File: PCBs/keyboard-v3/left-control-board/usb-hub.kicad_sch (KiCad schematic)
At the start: 16 parts, among them U101 USB2534-1080AEN, U801 NCP380HMU05AATBG, Y101 CX2016SA24000D0HLLG3

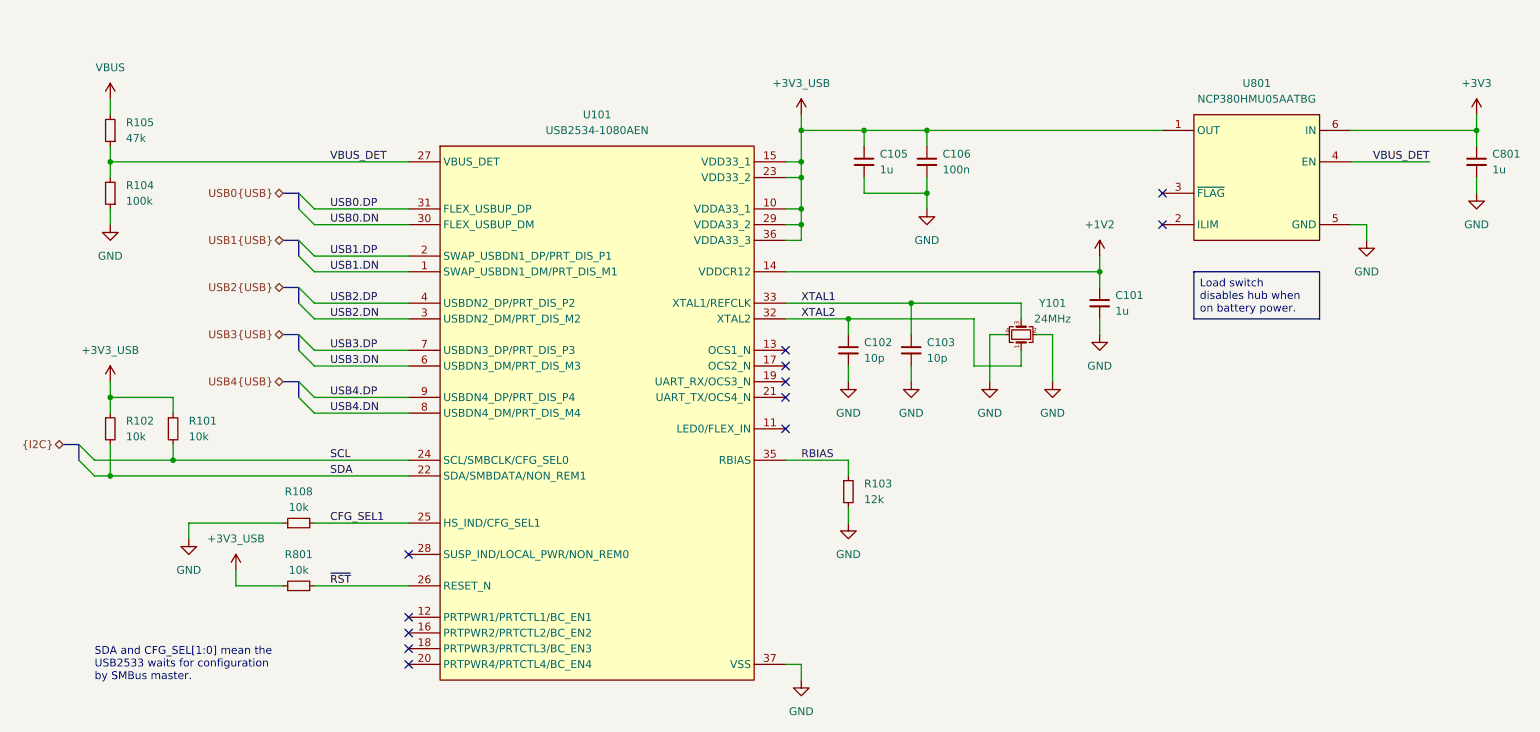
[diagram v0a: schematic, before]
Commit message: Added debug-breakout board, progress on right side schematics & layout
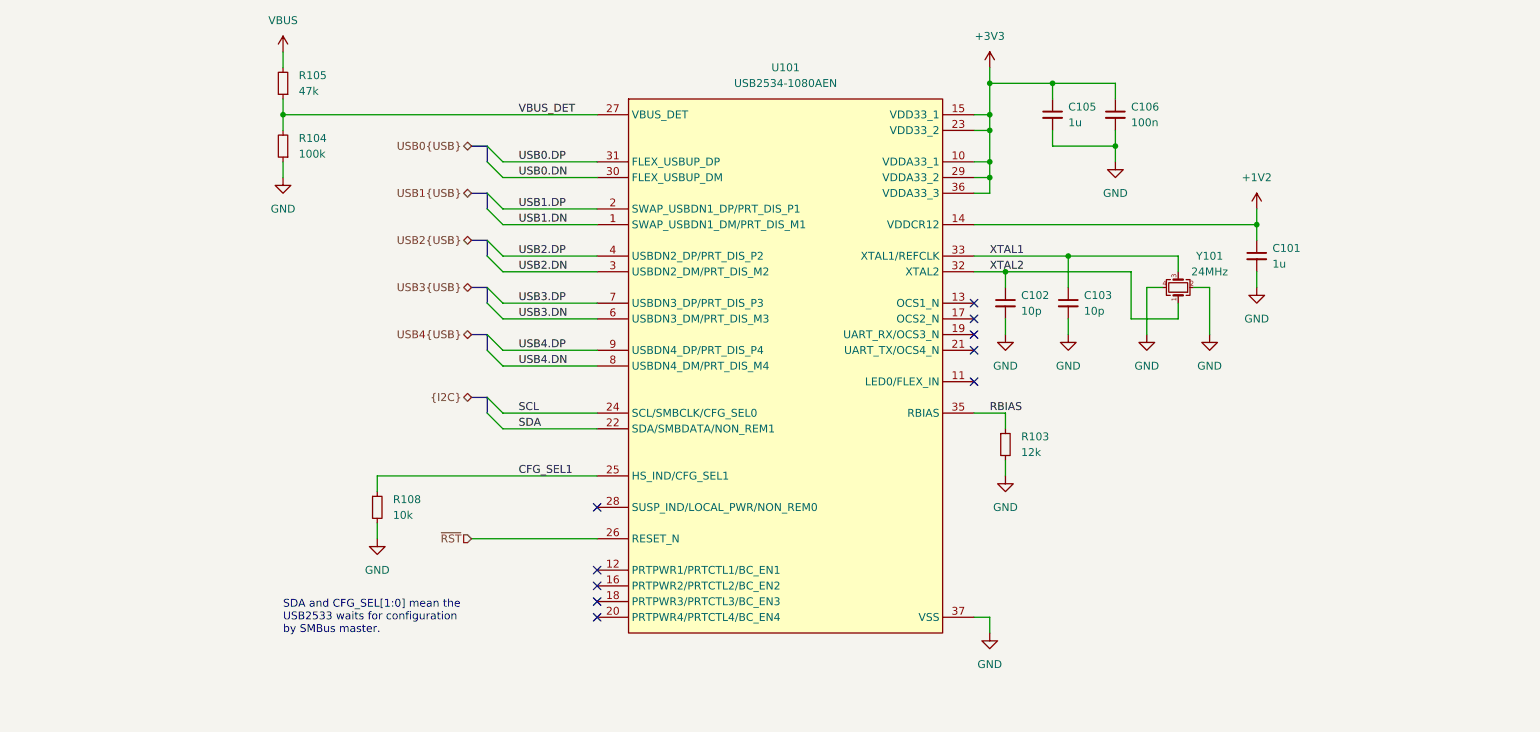
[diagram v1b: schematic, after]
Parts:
- removed C801: 1u, project_footprints:C_0402, symbol DEV:C_SMALL
- removed R101, R102, R801: 10k, project_footprints:R_0402, symbol DEV:R_SMALL
- removed U801: NCP380HMU05AATBG, project_footprints:SON65P200X200X55-7N, symbol PWR-SWCH:NCP380HMU05AATBG
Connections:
- net +3V3_USB is gone; now on net +3V3: C105.1, C106.1, U101.10 (VDDA33_1), U101.15 (VDD33_1), U101.23 (VDD33_2), U101.29 (VDDA33_2), U101.36 (VDDA33_3)
- net CFG_SEL1: now also R108.1; no longer R108.2
- net GND: now also R108.2; no longer R108.1
- no-connect marks 12 -> 10
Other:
- moved on the sheet: C101, C102, C103, C105, C106, R103, R104, R105, R108, U101, Y101

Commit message: Left knob board done
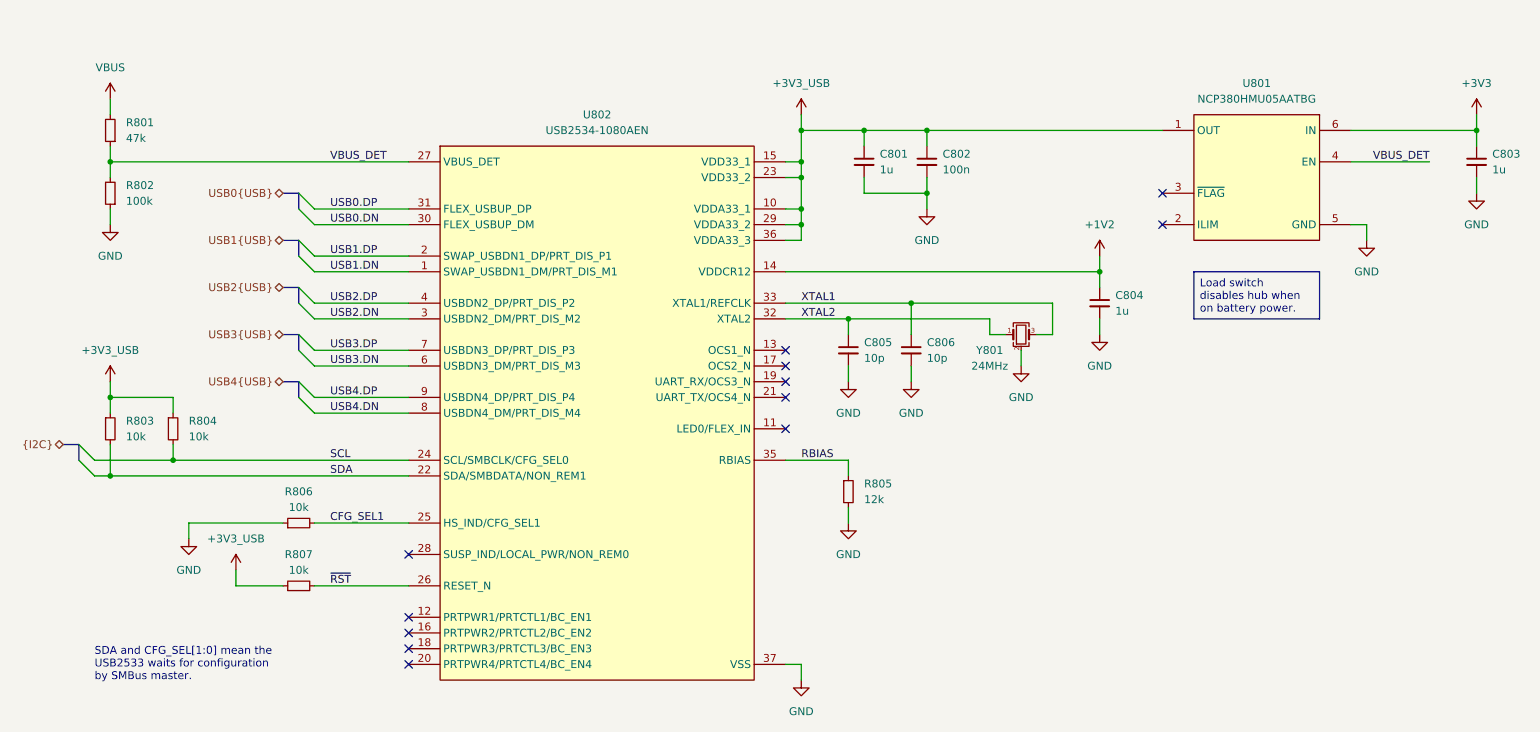
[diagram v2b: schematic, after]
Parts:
- added C803: 1u, project_footprints:C_0402, symbol DEV:C_SMALL
- added R803, R804, R807: 10k, project_footprints:R_0402, symbol DEV:R_SMALL
- added U801: NCP380HMU05AATBG, project_footprints:SON65P200X200X55-7N, symbol PWR-SWCH:NCP380HMU05AATBG
- U802: renamed from U101; footprint QFN50P600X600X100-37N-D -> project_footprints:QFN50P600X600X100-37N-D
- renumbered C105 to C801, C106 to C802, C101 to C804, C102 to C805, C103 to C806, R105 to R801, R104 to R802, R103 to R805, R108 to R806, Y101 to Y801
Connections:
- net +3V3: now also C803.1, U801.6 (IN); no longer C801.1, C802.1, U802.10 (VDDA33_1), U802.15 (VDD33_1), U802.23 (VDD33_2), U802.29 (VDDA33_2), U802.36 (VDDA33_3)
- net CFG_SEL1: now also R806.2; no longer R806.1
- net GND: now also R806.1, C803.2, U801.5 (GND), U801.7 (GND); no longer R806.2
- net SCL: now also R804.2
- net SDA: now also R803.2
- net VBUS_DET: now also U801.4 (EN)
- net ~{RST}: now also R807.2
- new net +3V3_USB: C801.1, C802.1, R803.1, R804.1, R807.1, U801.1 (OUT), U802.10 (VDDA33_1), U802.15 (VDD33_1), U802.23 (VDD33_2), U802.29 (VDDA33_2), U802.36 (VDDA33_3)
- no-connect marks 10 -> 12
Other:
- moved on the sheet: C801, C802, C804, C805, C806, R801, R802, R805, R806, U802
